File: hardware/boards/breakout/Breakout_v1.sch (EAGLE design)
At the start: 4 parts

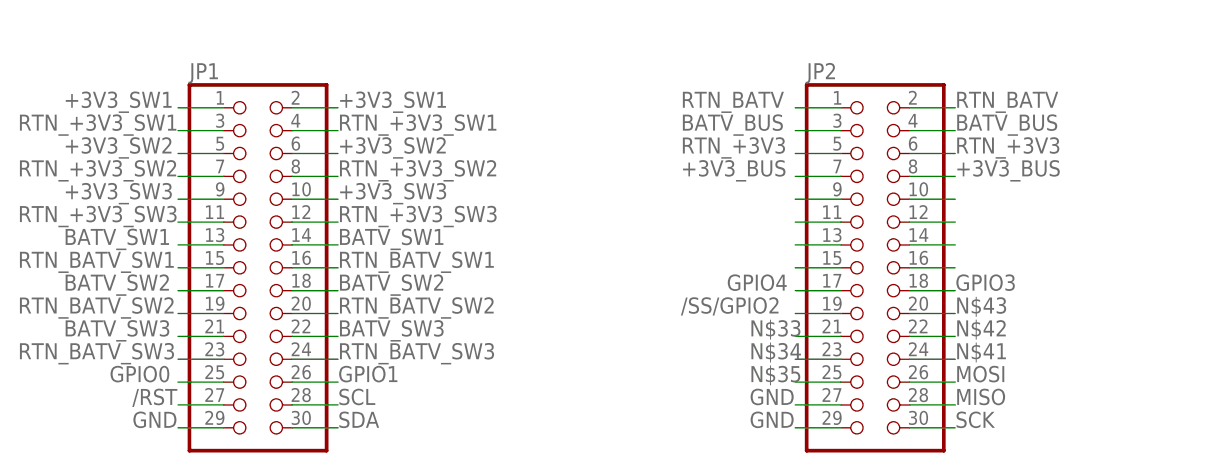
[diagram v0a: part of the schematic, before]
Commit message: Added V2 breakout ready to order
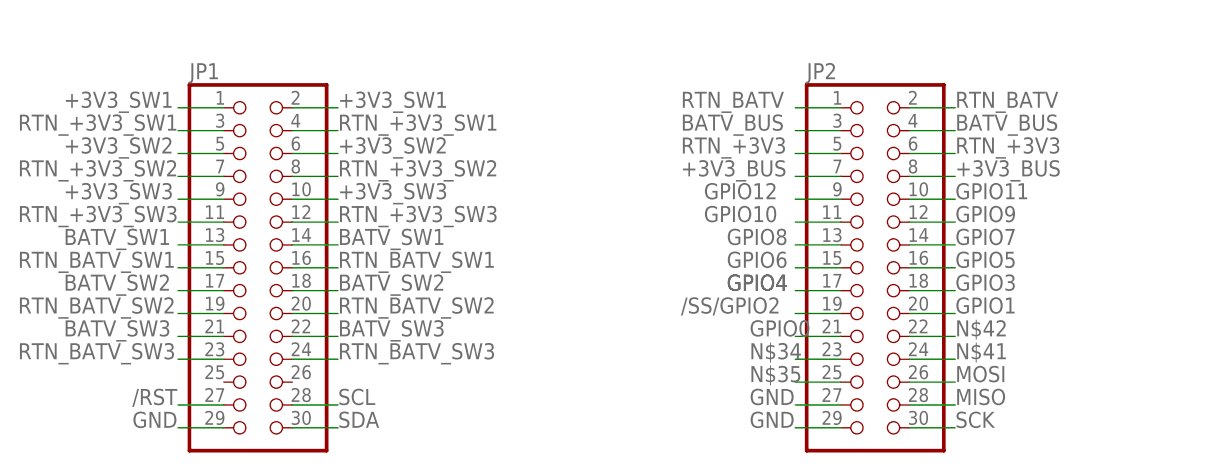
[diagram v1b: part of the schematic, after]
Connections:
- removed net N$33: JP2.21
- removed net N$43: JP2.20
- net GPIO0: now also JP2.21; no longer JP1.25
- net GPIO1: now also JP2.20; no longer JP1.26
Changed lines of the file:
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@@
 <?xml version="1.0" encoding="utf-8"?>
 <!DOCTYPE eagle SYSTEM "eagle.dtd">
-<eagle version="7.0.0">
+<eagle version="7.5.0">
 <drawing>
 <settings>
@@
 <schematic xreflabel="%F%N/%S.%C%R" xrefpart="/%S.%C%R">
 <attributes>
-<attribute name="CNAME" value="EARS PocketQube Template"/>
-<attribute name="CREVISION" value="0.1"/>
+<attribute name="CNAME" value="EARS PocketQube Breakout Board"/>
+<attribute name="CREVISION" value="1.0"/>
 <attribute name="DESIGNER" value="L. Stant"/>
 </attributes>
@@
 <pinref part="JP2" gate="A" pin="11"/>
 <wire x1="111.76" y1="30.48" x2="106.68" y2="30.48" width="0.1524" layer="91"/>
+<label x="96.52" y="30.48" size="1.778" layer="95"/>
 </segment>
 </net>
@@
 <pinref part="JP2" gate="A" pin="9"/>
 <wire x1="111.76" y1="33.02" x2="106.68" y2="33.02" width="0.1524" layer="91"/>
+<label x="96.52" y="33.02" size="1.778" layer="95"/>
 </segment>
 </net>
@@
 <pinref part="JP2" gate="A" pin="10"/>
 <wire x1="119.38" y1="33.02" x2="124.46" y2="33.02" width="0.1524" layer="91"/>
+<label x="124.46" y="33.02" size="1.778" layer="95"/>
 </segment>
 </net>
@@
 </segment>
 <segment>
-<pinref part="JP1" gate="A" pin="25"/>
-<wire x1="43.18" y1="12.7" x2="38.1" y2="12.7" width="0.1524" layer="91"/>
-<label x="30.48" y="12.7" size="1.778" layer="95"/>
+<pinref part="JP2" gate="A" pin="21"/>
+<wire x1="111.76" y1="17.78" x2="106.68" y2="17.78" width="0.1524" layer="91"/>
+<label x="101.6" y="17.78" size="1.778" layer="95"/>
 </segment>
 </net>
@@
 </segment>
 <segment>
-<pinref part="JP1" gate="A" pin="26"/>
-<wire x1="50.8" y1="12.7" x2="55.88" y2="12.7" width="0.1524" layer="91"/>
-<label x="55.88" y="12.7" size="1.778" layer="95"/>
+<pinref part="JP2" gate="A" pin="20"/>
+<wire x1="119.38" y1="20.32" x2="124.46" y2="20.32" width="0.1524" layer="91"/>
+<label x="124.46" y="20.32" size="1.778" layer="95"/>
 </segment>
 </net>
@@
 <pinref part="JP2" gate="A" pin="16"/>
 <wire x1="119.38" y1="25.4" x2="124.46" y2="25.4" width="0.1524" layer="91"/>
+<label x="124.46" y="25.4" size="1.778" layer="95"/>
 </segment>
 </net>
@@
 <wire x1="111.76" y1="22.86" x2="106.68" y2="22.86" width="0.1524" layer="91"/>
 <label x="99.06" y="22.86" size="1.778" layer="95"/>
+<label x="99.06" y="22.86" size="1.778" layer="95"/>
 </segment>
 </net>
@@
 <pinref part="JP2" gate="A" pin="13"/>
 <wire x1="111.76" y1="27.94" x2="106.68" y2="27.94" width="0.1524" layer="91"/>
+<label x="99.06" y="27.94" size="1.778" layer="95"/>
 </segment>
 </net>
@@
 <pinref part="JP2" gate="A" pin="14"/>
 <wire x1="119.38" y1="27.94" x2="124.46" y2="27.94" width="0.1524" layer="91"/>
+<label x="124.46" y="27.94" size="1.778" layer="95"/>
 </segment>
 </net>
@@
 <pinref part="JP2" gate="A" pin="15"/>
 <wire x1="111.76" y1="25.4" x2="106.68" y2="25.4" width="0.1524" layer="91"/>
+<label x="99.06" y="25.4" size="1.778" layer="95"/>
 </segment>
 </net>
@@
 <pinref part="JP2" gate="A" pin="12"/>
 <wire x1="119.38" y1="30.48" x2="124.46" y2="30.48" width="0.1524" layer="91"/>
+<label x="124.46" y="30.48" size="1.778" layer="95"/>
 </segment>
 </net>
@@
 </segment>
 </net>
-<net name="N$33" class="0">
-<segment>
-<pinref part="JP2" gate="A" pin="21"/>
-<wire x1="111.76" y1="17.78" x2="106.68" y2="17.78" width="0.1524" layer="91"/>
-<label x="101.6" y="17.78" size="1.778" layer="95"/>
-</segment>
-</net>
 <net name="N$34" class="0">
 <segment>
@@
 </segment>
 </net>
-<net name="N$43" class="0">
-<segment>
-<pinref part="JP2" gate="A" pin="20"/>
-<wire x1="119.38" y1="20.32" x2="124.46" y2="20.32" width="0.1524" layer="91"/>
-<label x="124.46" y="20.32" size="1.778" layer="95"/>
-</segment>
-</net>
